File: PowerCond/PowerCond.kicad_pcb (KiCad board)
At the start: 2 copper layers, 208.3 x 48.3 mm, 42 parts, among them J1 Conn_01x02, J10 Conn_01x01, J11 Conn_01x01, J12 Conn_01x01, J2 Conn_01x02, J3 Conn_01x02, J4 Conn_01x02, J5 Conn_01x02, J6 Conn_01x02, J7 Conn_01x02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

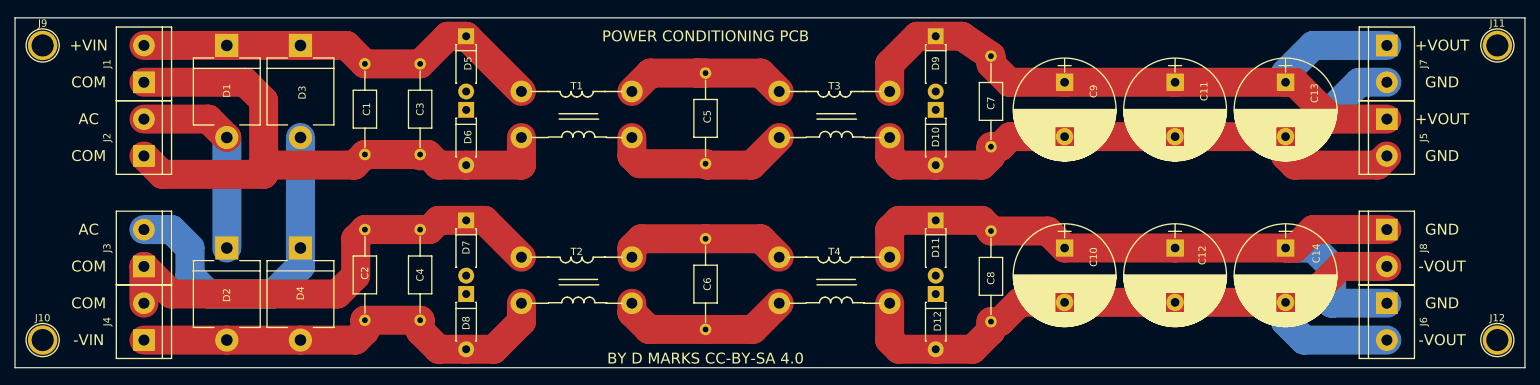
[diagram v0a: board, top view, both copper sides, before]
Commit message: Added XLRtoBal
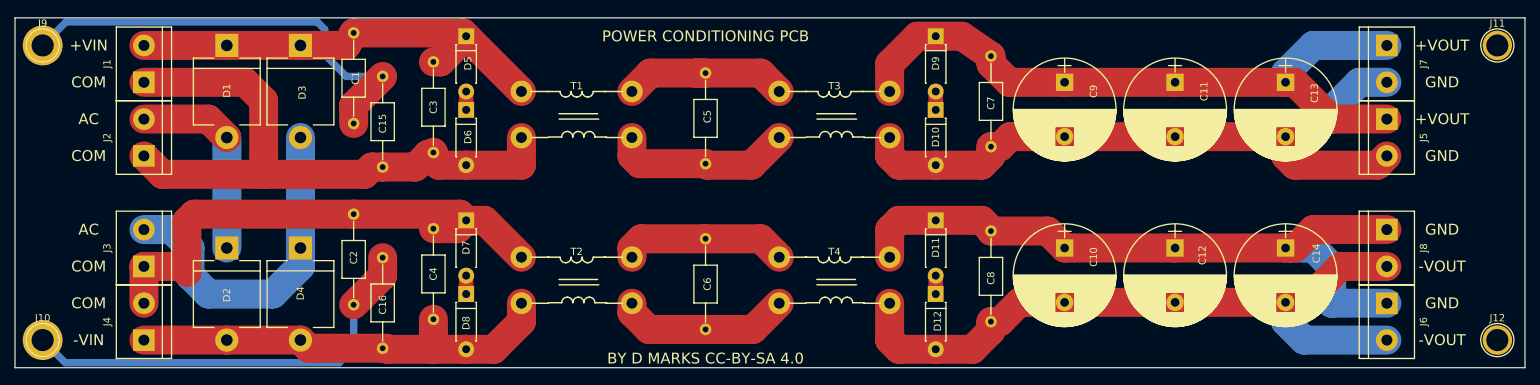
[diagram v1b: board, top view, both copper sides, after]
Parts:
- added C15: 1 uF, Capacitors_THT:C_Axial_L5.1mm_D3.1mm_P12.50mm_Horizontal, F.Cu at (86.3, 53.8)
- added C16: 1 uF, Capacitors_THT:C_Axial_L5.1mm_D3.1mm_P12.50mm_Horizontal, F.Cu at (86.3, 78.8)
- moved C1 4.54 mm to (82.3, 47.8)
- moved C2 2.63 mm to (82.3, 72.8)
- moved C3 1.85 mm to (93.3, 51.8)
- moved C4 1.83 mm to (93.3, 74.8)
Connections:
- C2 pad 2: Net-(C2-Pad2) -> Net-(C16-Pad1)
- C3 pad 2: Net-(C1-Pad2) -> Net-(C15-Pad2)
- C4 pad 2: Net-(C2-Pad2) -> Net-(C16-Pad2)
- D2 pad 2: Net-(C2-Pad2) -> Net-(C16-Pad2)
- D4 pad 2: Net-(C2-Pad2) -> Net-(C16-Pad2)
- D6 pad 2: Net-(C1-Pad2) -> Net-(C15-Pad2)
- D8 pad 2: Net-(C2-Pad2) -> Net-(C16-Pad2)
- J1 pad 1: Net-(C1-Pad2) -> Net-(C15-Pad2)
- J10 pad 1: (no net) -> Net-(C16-Pad1)
- J2 pad 1: Net-(C1-Pad2) -> Net-(C15-Pad2)
- J4 pad 1: Net-(C2-Pad2) -> Net-(C16-Pad2)
- J9 pad 1: (no net) -> Net-(C1-Pad2)
- T1 pad 4: Net-(C1-Pad2) -> Net-(C15-Pad2)
- T2 pad 4: Net-(C2-Pad2) -> Net-(C16-Pad2)
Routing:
- net Net-(C15-Pad2): track 0.00 -> 87.4 mm
- net Net-(C16-Pad2): track 0.00 -> 62.1 mm
- net Net-(C2-Pad2): track 60.7 -> 0.00 mm
- net Net-(C16-Pad1): track 0.00 -> 59.2 mm
- net Net-(C1-Pad2): track 86.1 -> 61.6 mm
- net Net-(C1-Pad1): track 57.9 -> 62.4 mm
- net Net-(C2-Pad1): track 68.0 -> 72.3 mm
- net Net-(D5-Pad2): track 0.00 -> 2.54 mm
- net Net-(D10-Pad1): track 0.00 -> 2.54 mm
- net Net-(D7-Pad2): track 0.00 -> 2.54 mm
- net Net-(D11-Pad2): track 0.00 -> 2.54 mm

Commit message: Added soft start circuit
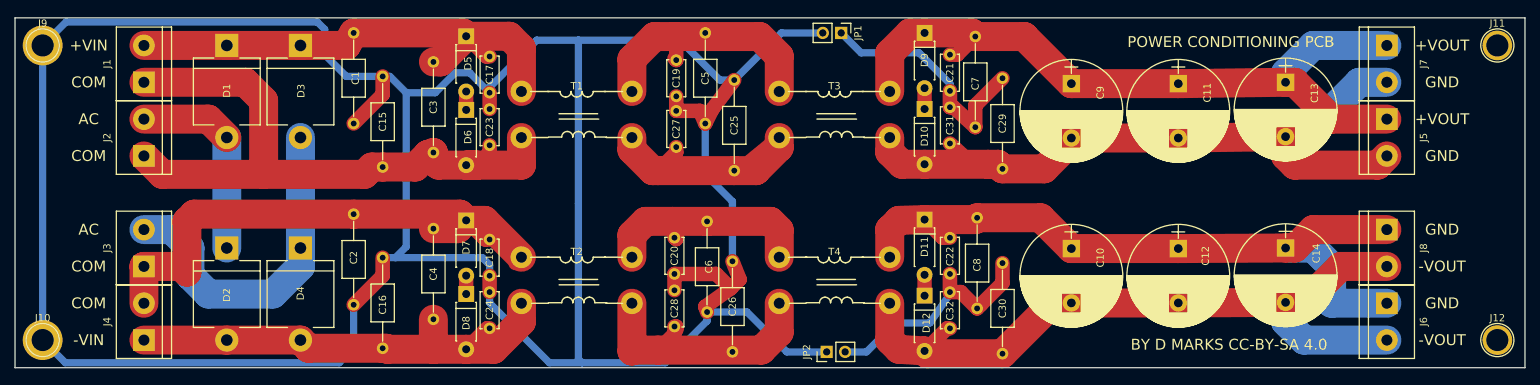
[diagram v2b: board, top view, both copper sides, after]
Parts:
- added C17: 1 nF, Capacitors_THT:C_Disc_D5.0mm_W2.5mm_P5.00mm, F.Cu at (101.0, 51.0)
- added C18: 1 nF, Capacitors_THT:C_Disc_D5.0mm_W2.5mm_P5.00mm, F.Cu at (101.0, 76.3)
- added C19: 1 nF, Capacitors_THT:C_Disc_D5.0mm_W2.5mm_P5.00mm, F.Cu at (126.8, 51.5)
- added C20: 1 nF, Capacitors_THT:C_Disc_D5.0mm_W2.5mm_P5.00mm, F.Cu at (126.5, 76.0)
- added C21: 1 nF, Capacitors_THT:C_Disc_D5.0mm_W2.5mm_P5.00mm, F.Cu at (164.5, 50.8)
- added C22: 1 nF, Capacitors_THT:C_Disc_D5.0mm_W2.5mm_P5.00mm, F.Cu at (164.5, 76.0)
- added C23: 1 nF, Capacitors_THT:C_Disc_D5.0mm_W2.5mm_P5.00mm, F.Cu at (101.0, 58.3)
- added C24: 1 nF, Capacitors_THT:C_Disc_D5.0mm_W2.5mm_P5.00mm, F.Cu at (101.0, 83.5)
- added C25: 1 uF, Capacitors_THT:C_Axial_L5.1mm_D3.1mm_P12.50mm_Horizontal, F.Cu at (134.8, 54.3)
- added C26: 1 uF, Capacitors_THT:C_Axial_L5.1mm_D3.1mm_P12.50mm_Horizontal, F.Cu at (134.5, 79.3)
- added C27: 1 nF, Capacitors_THT:C_Disc_D5.0mm_W2.5mm_P5.00mm, F.Cu at (126.8, 58.5)
- added C28: 1 nF, Capacitors_THT:C_Disc_D5.0mm_W2.5mm_P5.00mm, F.Cu at (126.5, 83.3)
- added C29: 1 uF, Capacitors_THT:C_Axial_L5.1mm_D3.1mm_P12.50mm_Horizontal, F.Cu at (171.8, 66.5)
- added C30: 1 uF, Capacitors_THT:C_Axial_L5.1mm_D3.1mm_P12.50mm_Horizontal, F.Cu at (171.8, 92.0)
- added C31: 1 nF, Capacitors_THT:C_Disc_D5.0mm_W2.5mm_P5.00mm, F.Cu at (164.5, 58.0)
- added C32: 1 nF, Capacitors_THT:C_Disc_D5.0mm_W2.5mm_P5.00mm, F.Cu at (164.5, 83.5)
- added JP1: Jumper_NC_Small, Pin_Headers:Pin_Header_Straight_1x02_Pitch2.54mm, F.Cu at (149.5, 47.8)
- added JP2: Jumper_NC_Small, Pin_Headers:Pin_Header_Straight_1x02_Pitch2.54mm, F.Cu at (147.5, 91.8)
- moved C5 5.54 mm to (130.8, 47.8)
- moved C7 3.46 mm to (168.0, 60.8)
- moved C8 2.65 mm to (168.3, 85.8)
- moved C6 2.41 mm to (131.0, 73.8)
- moved D9 1.61 mm to (161.0, 47.8)
- moved D12 1.56 mm to (161.0, 84.0)
- moved D10 1.54 mm to (161.0, 58.3)
- moved D11 1.54 mm to (161.0, 73.5)
- moved C9 0.95 mm to (181.3, 54.8)
- moved C10 0.93 mm to (181.3, 77.5)
- moved C11 0.48 mm to (196.0, 54.8)
- moved C12 0.45 mm to (196.0, 77.5)
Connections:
- C16 pad 1: Net-(C16-Pad1) -> Net-(C1-Pad2)
- C2 pad 2: Net-(C16-Pad1) -> Net-(C1-Pad2)
- C5 pad 2: Net-(C5-Pad2) -> Net-(C1-Pad2)
- C6 pad 2: Net-(C6-Pad2) -> Net-(C1-Pad2)
- C7 pad 1: Net-(C11-Pad2) -> Net-(C21-Pad2)
- C8 pad 1: Net-(C10-Pad2) -> Net-(C22-Pad2)
- J10 pad 1: Net-(C16-Pad1) -> Net-(C1-Pad2)
- T1 pad 3: Net-(C5-Pad2) -> Net-(C25-Pad2)
- T2 pad 3: Net-(C6-Pad2) -> Net-(C26-Pad2)
- T3 pad 4: Net-(C5-Pad2) -> Net-(C25-Pad2)
- T4 pad 4: Net-(C6-Pad2) -> Net-(C26-Pad2)
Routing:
- net Net-(C1-Pad2): track 61.6 -> 435.6 mm
- net Net-(C16-Pad1): track 59.2 -> 0.00 mm
- net Net-(C26-Pad2): track 0.00 -> 44.6 mm
- net Net-(C25-Pad2): track 0.00 -> 38.0 mm
- net Net-(C21-Pad2): track 0.00 -> 34.8 mm
- net Net-(C22-Pad2): track 0.00 -> 33.4 mm
- net Net-(C5-Pad2): track 25.0 -> 0.00 mm
- net Net-(C19-Pad1): track 23.7 -> 47.8 mm
- net Net-(C6-Pad2): track 24.1 -> 0.00 mm
- net Net-(C20-Pad1): track 23.2 -> 32.1 mm
- net Net-(C1-Pad1): track 62.4 -> 70.5 mm
- net Net-(C11-Pad2): track 94.8 -> 101.7 mm
- net Net-(C15-Pad2): track 87.4 -> 93.8 mm
- net Net-(C11-Pad1): track 95.9 -> 101.4 mm
- net Net-(C18-Pad1): track 72.3 -> 77.8 mm
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
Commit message: Changed softstart and Poweramp to TO-220 transistors
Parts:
- removed C3, C4: 1 uF, Capacitors_THT:C_Axial_L5.1mm_D3.1mm_P12.50mm_Horizontal
- D10, D11, D12, D5, D6, D7, D8, D9: value 1N4477 -> 1N4755A
- moved C15 5.52 mm to (91.8, 53.3)
- moved C16 5.52 mm to (91.8, 79.3)
- moved C1 4.00 mm to (86.3, 47.8)
- moved C2 4.00 mm to (86.3, 72.8)
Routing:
- net Net-(C1-Pad2): track 435.6 -> 478.3 mm
- net Net-(C1-Pad1): track 70.5 -> 63.4 mm
- net Net-(C16-Pad2): track 67.3 -> 62.2 mm
- net Net-(C15-Pad2): track 93.8 -> 90.3 mm

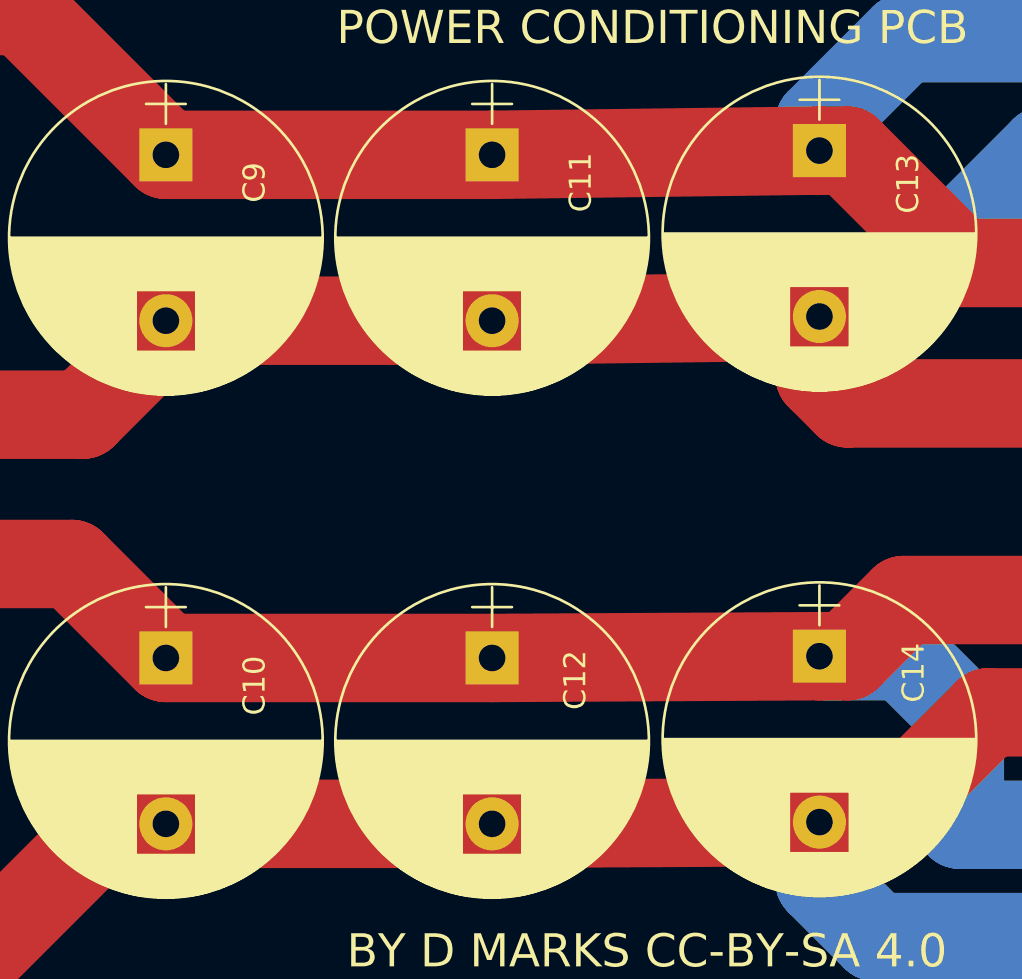
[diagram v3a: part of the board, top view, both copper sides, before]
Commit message: Changed to 2N5551/2N5401 from BC546C/BC556C transistors
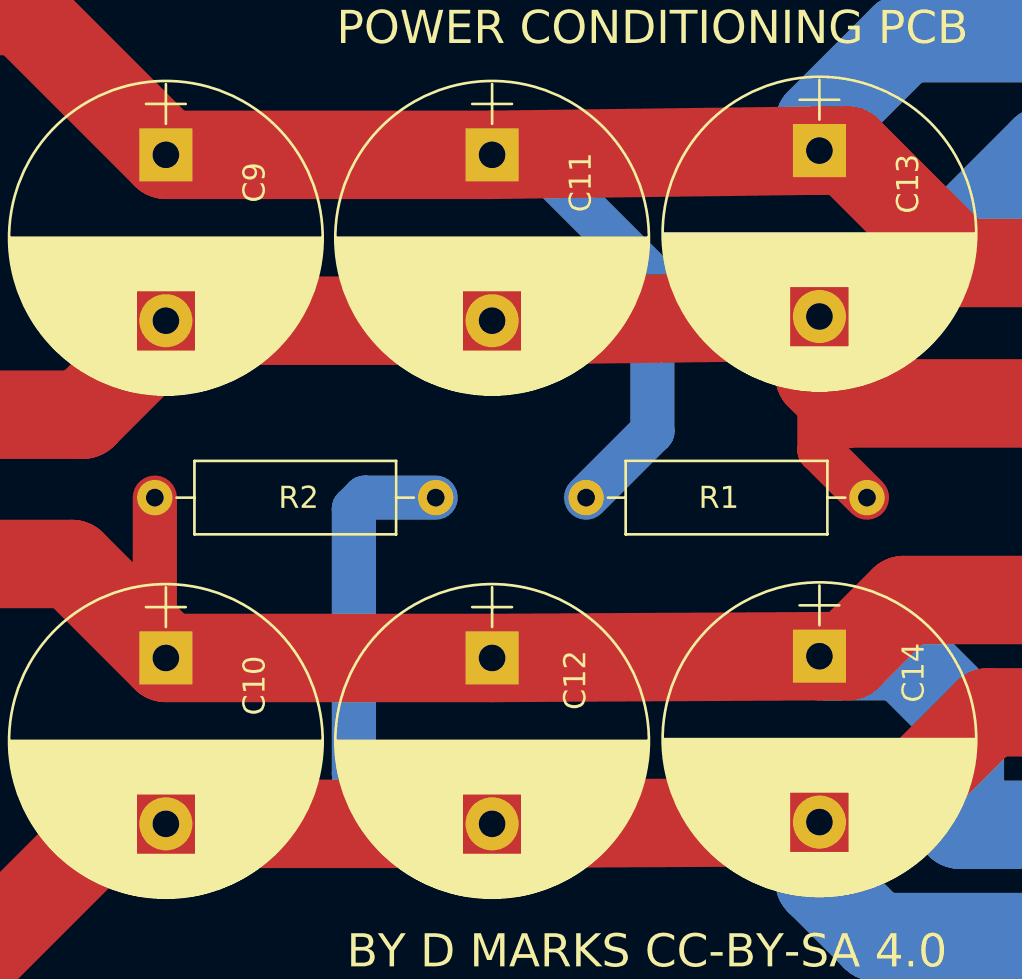
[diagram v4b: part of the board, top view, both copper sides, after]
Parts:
- added R1: 220k, Resistors_THT:R_Axial_DIN0309_L9.0mm_D3.2mm_P12.70mm_Horizontal, F.Cu at (200.3, 70.3)
- added R2: 220k, Resistors_THT:R_Axial_DIN0309_L9.0mm_D3.2mm_P12.70mm_Horizontal, F.Cu at (180.8, 70.3)
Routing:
- net Net-(C10-Pad2): track 101.8 -> 124.9 mm
- net Net-(C11-Pad1): track 101.4 -> 122.1 mm
- net Net-(C11-Pad2): track 101.7 -> 110.7 mm
- net Net-(C10-Pad1): track 100.5 -> 107.9 mm
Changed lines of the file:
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@@
 (kicad_pcb (version 4) (host pcbnew 4.0.7)
   (general
-    (links 101)
+    (links 105)
     (no_connects 0)
     (area 35.484999 45.644999 243.915001 94.055001)
     (thickness 1.6)
     (drawings 22)
-    (tracks 283)
+    (tracks 296)
     (zones 0)
-    (modules 60)
+    (modules 62)
     (nets 22)
   )
@@
   )
   (setup
-    (last_trace_width 1)
+    (last_trace_width 2)
     (user_trace_width 0.5)
     (user_trace_width 1)
@@
     )
   )
+  (module Resistors_THT:R_Axial_DIN0309_L9.0mm_D3.2mm_P12.70mm_Horizontal (layer F.Cu)
+    (at 200.27 70.3)
+    (descr "Resistor, Axial_DIN0309 series, Axial, Horizontal, pin pitch=12.7mm, 0.5W = 1/2W, length*diameter=9*3.2mm^2, http://cdn-reichelt.de/documents/datenblatt/B400/1_4W%23YAG.pdf")
+    (tags "Resistor Axial_DIN0309 series Axial Horizontal pin pitch 12.7mm 0.5W = 1/2W length 9mm diameter 3.2mm")
+    (fp_text reference R1 (at 6 0) (layer F.SilkS)
+      (effects (font (size 1 1) (thickness 0.15)))
+    )
+    (fp_text value 220k (at 6.35 2.66) (layer F.Fab)
+      (effects (font (size 1 1) (thickness 0.15)))
+    )
+    (fp_line (start 1.85 -1.6) (end 1.85 1.6) (layer F.Fab) (width 0.1))
+    (fp_line (start 1.85 1.6) (end 10.85 1.6) (layer F.Fab) (width 0.1))
+    (fp_line (start 10.85 1.6) (end 10.85 -1.6) (layer F.Fab) (width 0.1))
+    (fp_line (start 10.85 -1.6) (end 1.85 -1.6) (layer F.Fab) (width 0.1))
+    (fp_line (start 0 0) (end 1.85 0) (layer F.Fab) (width 0.1))
+    (fp_line (start 12.7 0) (end 10.85 0) (layer F.Fab) (width 0.1))
+    (fp_line (start 1.79 -1.66) (end 1.79 1.66) (layer F.SilkS) (width 0.12))
+    (fp_line (start 1.79 1.66) (end 10.91 1.66) (layer F.SilkS) (width 0.12))
+    (fp_line (start 10.91 1.66) (end 10.91 -1.66) (layer F.SilkS) (width 0.12))
+    (fp_line (start 10.91 -1.66) (end 1.79 -1.66) (layer F.SilkS) (width 0.12))
+    (fp_line (start 0.98 0) (end 1.79 0) (layer F.SilkS) (width 0.12))
+    (fp_line (start 11.72 0) (end 10.91 0) (layer F.SilkS) (width 0.12))
+    (fp_line (start -1.05 -1.95) (end -1.05 1.95) (layer F.CrtYd) (width 0.05))
+    (fp_line (start -1.05 1.95) (end 13.75 1.95) (layer F.CrtYd) (width 0.05))
+    (fp_line (start 13.75 1.95) (end 13.75 -1.95) (layer F.CrtYd) (width 0.05))
+    (fp_line (start 13.75 -1.95) (end -1.05 -1.95) (layer F.CrtYd) (width 0.05))
+    (pad 1 thru_hole circle (at 0 0) (size 1.6 1.6) (drill 0.8) (layers *.Cu *.Mask)
+      (net 4 "Net-(C11-Pad1)"))
+    (pad 2 thru_hole oval (at 12.7 0) (size 1.6 1.6) (drill 0.8) (layers *.Cu *.Mask)
+      (net 3 "Net-(C11-Pad2)"))
+    (model ${KISYS3DMOD}/Resistors_THT.3dshapes/R_Axial_DIN0309_L9.0mm_D3.2mm_P12.70mm_Horizontal.wrl
+      (at (xyz 0 0 0))
+      (scale (xyz 0.393701 0.393701 0.393701))
+      (rotate (xyz 0 0 0))
+    )
+  )
+  (module Resistors_THT:R_Axial_DIN0309_L9.0mm_D3.2mm_P12.70mm_Horizontal (layer F.Cu)
+    (at 180.77 70.3)
+    (descr "Resistor, Axial_DIN0309 series, Axial, Horizontal, pin pitch=12.7mm, 0.5W = 1/2W, length*diameter=9*3.2mm^2, http://cdn-reichelt.de/documents/datenblatt/B400/1_4W%23YAG.pdf")
+    (tags "Resistor Axial_DIN0309 series Axial Horizontal pin pitch 12.7mm 0.5W = 1/2W length 9mm diameter 3.2mm")
+    (fp_text reference R2 (at 6.5 0) (layer F.SilkS)
+      (effects (font (size 1 1) (thickness 0.15)))
+    )
+    (fp_text value 220k (at 6.35 2.66) (layer F.Fab)
+      (effects (font (size 1 1) (thickness 0.15)))
+    )
+    (fp_line (start 1.85 -1.6) (end 1.85 1.6) (layer F.Fab) (width 0.1))
+    (fp_line (start 1.85 1.6) (end 10.85 1.6) (layer F.Fab) (width 0.1))
+    (fp_line (start 10.85 1.6) (end 10.85 -1.6) (layer F.Fab) (width 0.1))
+    (fp_line (start 10.85 -1.6) (end 1.85 -1.6) (layer F.Fab) (width 0.1))
+    (fp_line (start 0 0) (end 1.85 0) (layer F.Fab) (width 0.1))
+    (fp_line (start 12.7 0) (end 10.85 0) (layer F.Fab) (width 0.1))
+    (fp_line (start 1.79 -1.66) (end 1.79 1.66) (layer F.SilkS) (width 0.12))
+    (fp_line (start 1.79 1.66) (end 10.91 1.66) (layer F.SilkS) (width 0.12))
+    (fp_line (start 10.91 1.66) (end 10.91 -1.66) (layer F.SilkS) (width 0.12))
+    (fp_line (start 10.91 -1.66) (end 1.79 -1.66) (layer F.SilkS) (width 0.12))
+    (fp_line (start 0.98 0) (end 1.79 0) (layer F.SilkS) (width 0.12))
+    (fp_line (start 11.72 0) (end 10.91 0) (layer F.SilkS) (width 0.12))
+    (fp_line (start -1.05 -1.95) (end -1.05 1.95) (layer F.CrtYd) (width 0.05))
+    (fp_line (start -1.05 1.95) (end 13.75 1.95) (layer F.CrtYd) (width 0.05))
+    (fp_line (start 13.75 1.95) (end 13.75 -1.95) (layer F.CrtYd) (width 0.05))
+    (fp_line (start 13.75 -1.95) (end -1.05 -1.95) (layer F.CrtYd) (width 0.05))
+    (pad 1 thru_hole circle (at 0 0) (size 1.6 1.6) (drill 0.8) (layers *.Cu *.Mask)
+      (net 6 "Net-(C10-Pad1)"))
+    (pad 2 thru_hole oval (at 12.7 0) (size 1.6 1.6) (drill 0.8) (layers *.Cu *.Mask)
+      (net 5 "Net-(C10-Pad2)"))
+    (model ${KISYS3DMOD}/Resistors_THT.3dshapes/R_Axial_DIN0309_L9.0mm_D3.2mm_P12.70mm_Horizontal.wrl
+      (at (xyz 0 0 0))
+      (scale (xyz 0.393701 0.393701 0.393701))
+      (rotate (xyz 0 0 0))
+    )
+  )
   (gr_line (start 35.56 45.72) (end 243.84 45.72) (angle 90) (layer Edge.Cuts) (width 0.15))
   (gr_text "POWER CONDITIONING PCB" (at 203.27 49.05) (layer F.SilkS)
@@
   (segment (start 82.27 91.3) (end 80.27 93.3) (width 1) (layer B.Cu) (net 2))
   (segment (start 113.27 71.3) (end 113.27 92.8) (width 1) (layer B.Cu) (net 2))
+  (segment (start 210.82 62.11) (end 210.82 68.15) (width 2) (layer F.Cu) (net 3) (status 400000))
+  (segment (start 210.82 68.15) (end 212.97 70.3) (width 2) (layer F.Cu) (net 3) (status 800000))
   (segment (start 164.52 63.05) (end 167.64 65.92) (width 2) (layer F.Cu) (net 3) (status 10))
   (segment (start 169.77 66.55) (end 169.77 65.92) (width 2) (layer F.Cu) (net 3))
@@
   (segment (start 196.02 62.3) (end 210.82 62.11) (width 4) (layer F.Cu) (net 3) (status 10))
   (segment (start 181.27 62.3) (end 196.02 62.3) (width 4) (layer F.Cu) (net 3) (status 10))
+  (segment (start 196.02 54.8) (end 197.77 54.8) (width 2) (layer B.Cu) (net 4) (status 400000))
+  (segment (start 203.27 67.3) (end 200.27 70.3) (width 2) (layer B.Cu) (net 4) (status 800000))
+  (segment (start 203.27 60.3) (end 203.27 67.3) (width 2) (layer B.Cu) (net 4))
+  (segment (start 197.77 54.8) (end 203.27 60.3) (width 2) (layer B.Cu) (net 4))
   (segment (start 164.52 50.8) (end 165.52 50.8) (width 2) (layer F.Cu) (net 4))
   (segment (start 165.52 50.8) (end 168.02 48.3) (width 2) (layer F.Cu) (net 4))
@@
   (segment (start 196.02 54.8) (end 210.82 54.61) (width 4) (layer F.Cu) (net 4) (status 10))
   (segment (start 181.27 54.8) (end 196.02 54.8) (width 4) (layer F.Cu) (net 4) (status 10))
+  (segment (start 193.47 70.3) (end 190.27 70.3) (width 2) (layer B.Cu) (net 5))
+  (segment (start 192.02 85.05) (end 196.02 85.05) (width 2) (layer B.Cu) (net 5))
+  (segment (start 189.77 82.8) (end 192.02 85.05) (width 2) (layer B.Cu) (net 5))
+  (segment (start 189.77 70.8) (end 189.77 82.8) (width 2) (layer B.Cu) (net 5))
+  (segment (start 190.27 70.3) (end 189.77 70.8) (width 2) (layer B.Cu) (net 5))
   (segment (start 171.77 92.05) (end 161.4 92.05) (width 4) (layer F.Cu) (net 5))
   (segment (start 161.4 92.05) (end 161.02 91.67) (width 4) (layer F.Cu) (net 5))
@@
   (segment (start 213.36 90.17) (end 224.79 90.17) (width 4) (layer B.Cu) (net 5))
   (segment (start 218.44 80.01) (end 224.79 80.01) (width 4) (layer F.Cu) (net 5))
+  (segment (start 180.77 70.3) (end 180.77 77.05) (width 2) (layer F.Cu) (net 6))
+  (segment (start 180.77 77.05) (end 181.27 77.55) (width 2) (layer F.Cu) (net 6))
   (segment (start 168.27 73.3) (end 177.02 73.3) (width 4) (layer F.Cu) (net 6))
   (segment (start 177.02 73.3) (end 181.27 77.55) (width 4) (layer F.Cu) (net 6))
